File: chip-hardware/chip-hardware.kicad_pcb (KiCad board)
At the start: 2 copper layers, 74.2 x 30.5 mm, 22 parts, among them J1 Barrel_Jack, J2 Screw_Terminal_01x02, J3 Conn_01x02, U1 TLV70033_SOT23-5, U2 LIS3DH, U3 INA260, U4 MCP9808_MSOP, U5 ESP32-WROOM-32

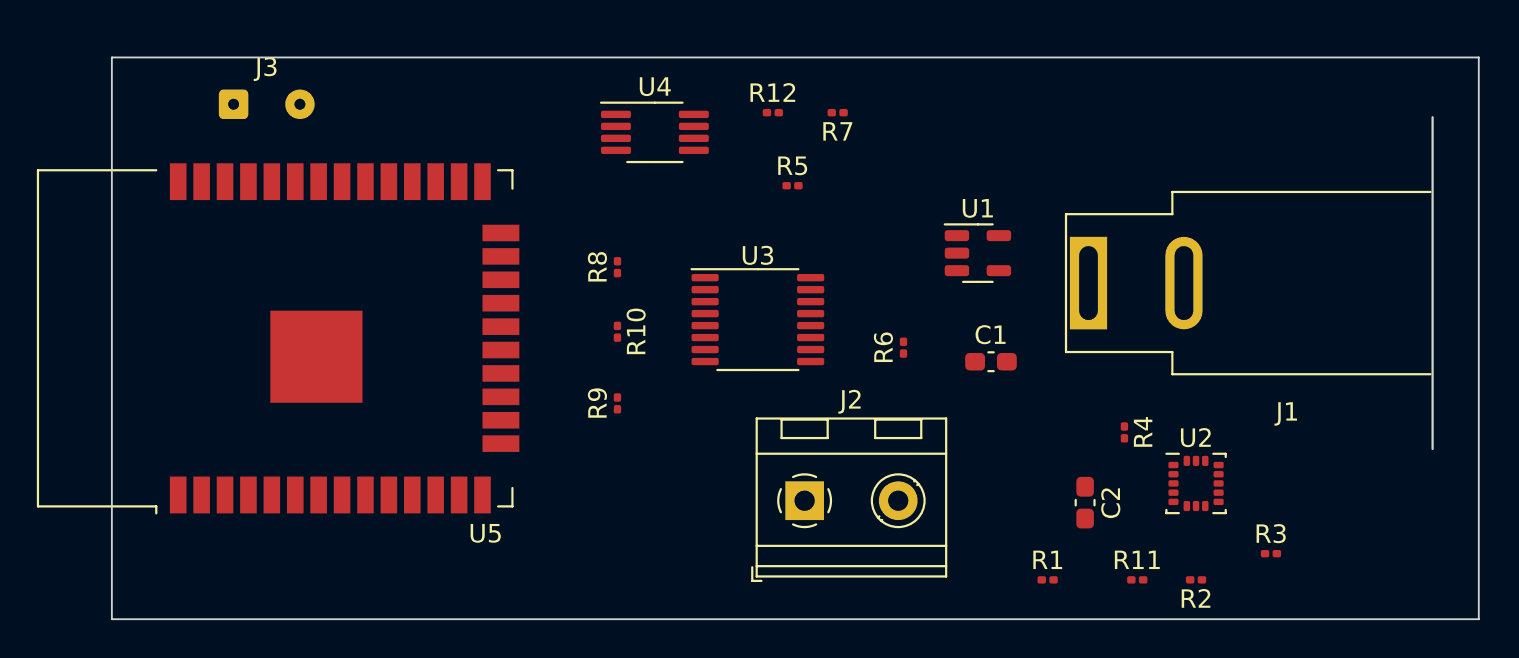
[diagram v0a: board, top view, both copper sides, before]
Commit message: Added corner radius to the chip
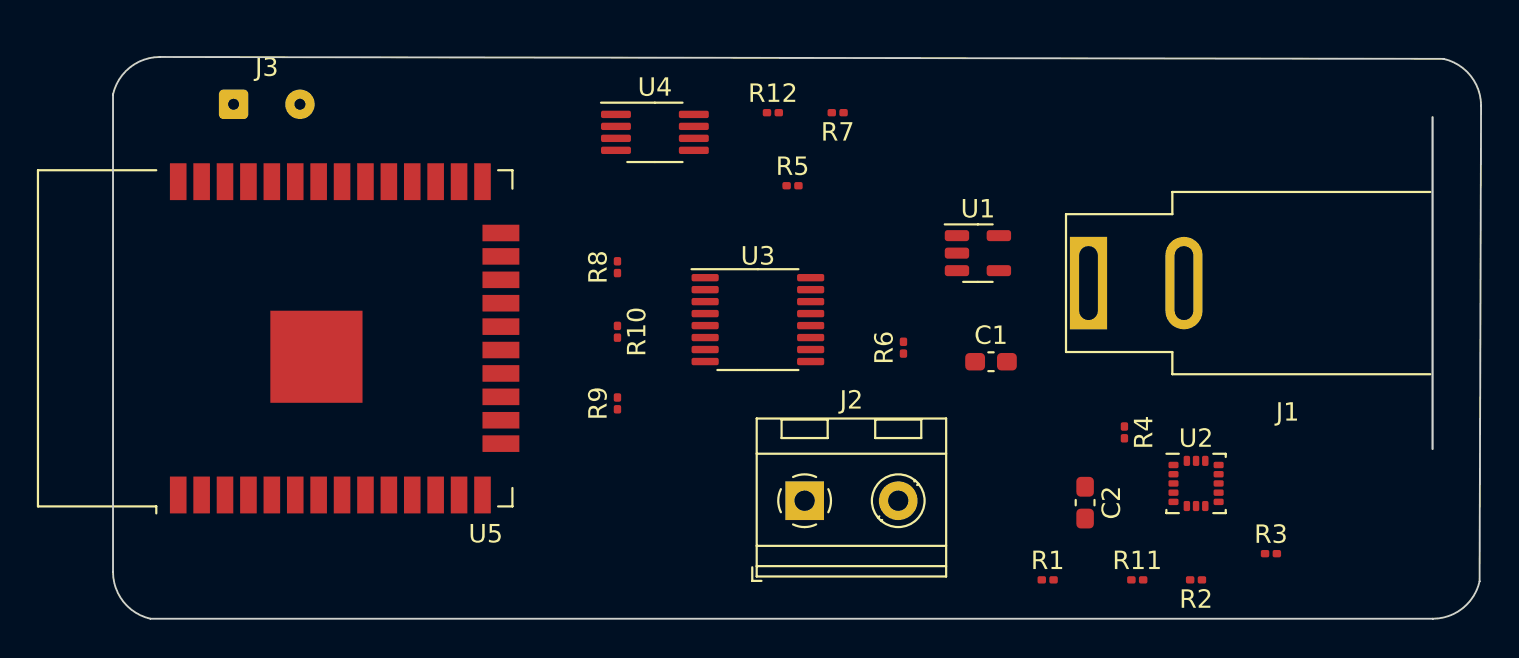
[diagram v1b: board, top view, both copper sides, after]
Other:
- outline, holes or cut-outs redrawn
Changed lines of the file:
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@@
     )
   )
-  (gr_rect (start 116.5246 86.1314) (end 190.6926 116.6114) (layer "Edge.Cuts") (width 0.1) (fill none))
+  (gr_arc (start 188.784508 86.208394) (mid 190.246 87.122) (end 190.816508 88.748394) (layer "Edge.Cuts") (width 0.1))
+  (gr_arc (start 190.735949 114.554) (mid 189.822343 116.015492) (end 188.195949 116.586) (layer "Edge.Cuts") (width 0.1))
+  (gr_arc (start 118.618 116.586) (mid 117.156508 115.672394) (end 116.586 114.046) (layer "Edge.Cuts") (width 0.1))
+  (gr_line (start 116.586 114.046) (end 116.586 88.138) (layer "Edge.Cuts") (width 0.1))
+  (gr_line (start 188.195949 116.586) (end 118.618 116.586) (layer "Edge.Cuts") (width 0.1))
+  (gr_line (start 190.735949 114.554) (end 190.816508 88.748394) (layer "Edge.Cuts") (width 0.1))
+  (gr_line (start 119.126 86.106) (end 188.784508 86.208394) (layer "Edge.Cuts") (width 0.1))
+  (gr_arc (start 116.586 88.138) (mid 117.499606 86.676508) (end 119.126 86.106) (layer "Edge.Cuts") (width 0.1))
 )

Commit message: more placement of parts
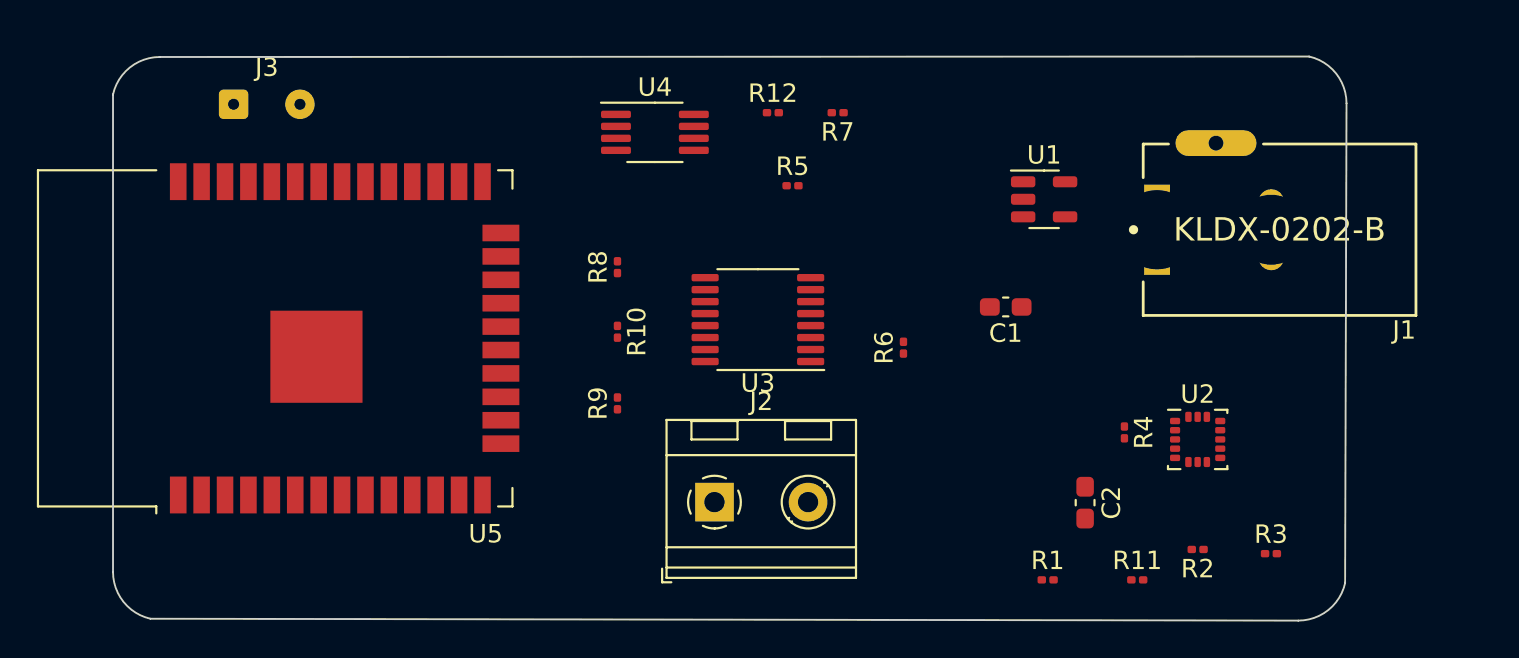
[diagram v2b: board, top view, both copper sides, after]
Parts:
- J1: value Barrel_Jack -> KLDX-0202-B; footprint Connector_BarrelJack:BarrelJack_SwitchcraftConxall_RAPC10U_Horizontal -> eec:Kycon-KLDX-0202-B-MFG
- moved J1 10.8 mm to (179.9, 95.5)
- moved J2 4.89 mm to (149.2, 110.3)
- moved U1 4.63 mm to (167.1, 93.8)
- moved C1 3.08 mm to (165.0, 99.7), turned to 180 degrees
- moved U2 2.39 mm to (175.4, 106.9)
- moved R2 1.65 mm to (175.4, 112.8)
- turned U3 to 180 degrees
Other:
- board size 74.2 x 30.5 mm -> 66.9 x 30.6 mm

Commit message: Got the traces mostly done. Just need to do some reviewing
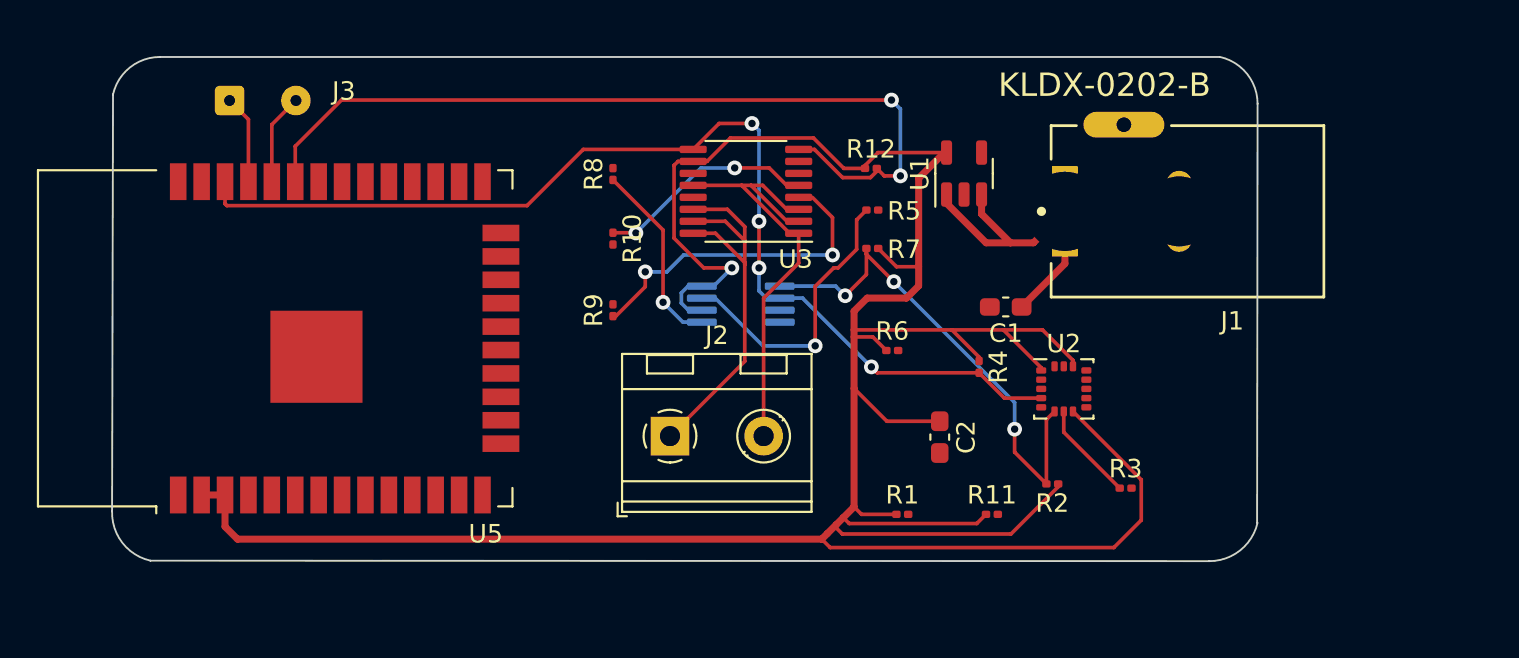
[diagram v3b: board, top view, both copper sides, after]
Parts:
- U4: moved to B.Cu
- moved U4 10.4 mm to (150.6, 99.5), turned to 180 degrees
- moved R2 8.65 mm to (167.6, 109.3)
- moved R1 8.65 mm to (159.4, 110.9)
- moved R3 8.65 mm to (171.5, 109.5)
- moved C2 8.65 mm to (161.4, 106.7)
- moved R11 8.65 mm to (164.3, 110.9)
- moved R4 8.65 mm to (163.6, 102.9)
- moved U2 7.77 mm to (168.2, 104.1)
- moved R7 7.60 mm to (157.8, 96.5)
- moved U3 6.99 mm to (150.9, 93.4)
- moved R12 6.12 mm to (157.7, 92.2)
- moved J1 5.09 mm to (174.9, 94.5)
- moved R9 5.06 mm to (143.7, 99.8)
- moved R10 5.06 mm to (143.7, 96.0)
- moved R8 5.06 mm to (143.7, 92.5)
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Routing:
- net +3V3: track 0.00 -> 168.1 mm, vias 0 -> 1
- net /SDA: track 0.00 -> 74.0 mm, vias 0 -> 5
- net /SCL: track 0.00 -> 58.6 mm, vias 0 -> 4
- net Net-(J2-Pad2): track 0.00 -> 25.6 mm
- net Net-(J2-Pad1): track 0.00 -> 23.0 mm
- net Net-(C1-Pad1): track 0.00 -> 17.9 mm
- net Net-(R9-Pad1): track 0.00 -> 17.3 mm, vias 0 -> 2
- net Net-(R5-Pad1): track 0.00 -> 15.9 mm, vias 0 -> 1
- net Net-(R10-Pad1): track 0.00 -> 11.9 mm, vias 0 -> 2
- net Net-(R8-Pad1): track 0.00 -> 10.3 mm, vias 0 -> 1
- net Net-(R3-Pad1): track 0.00 -> 5.42 mm
- net Net-(J3-Pad2): track 0.00 -> 4.94 mm
- net Net-(J3-Pad1): track 0.00 -> 4.83 mm
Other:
- board size 66.9 x 30.6 mm -> 62.2 x 27.4 mm

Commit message: filled the zones
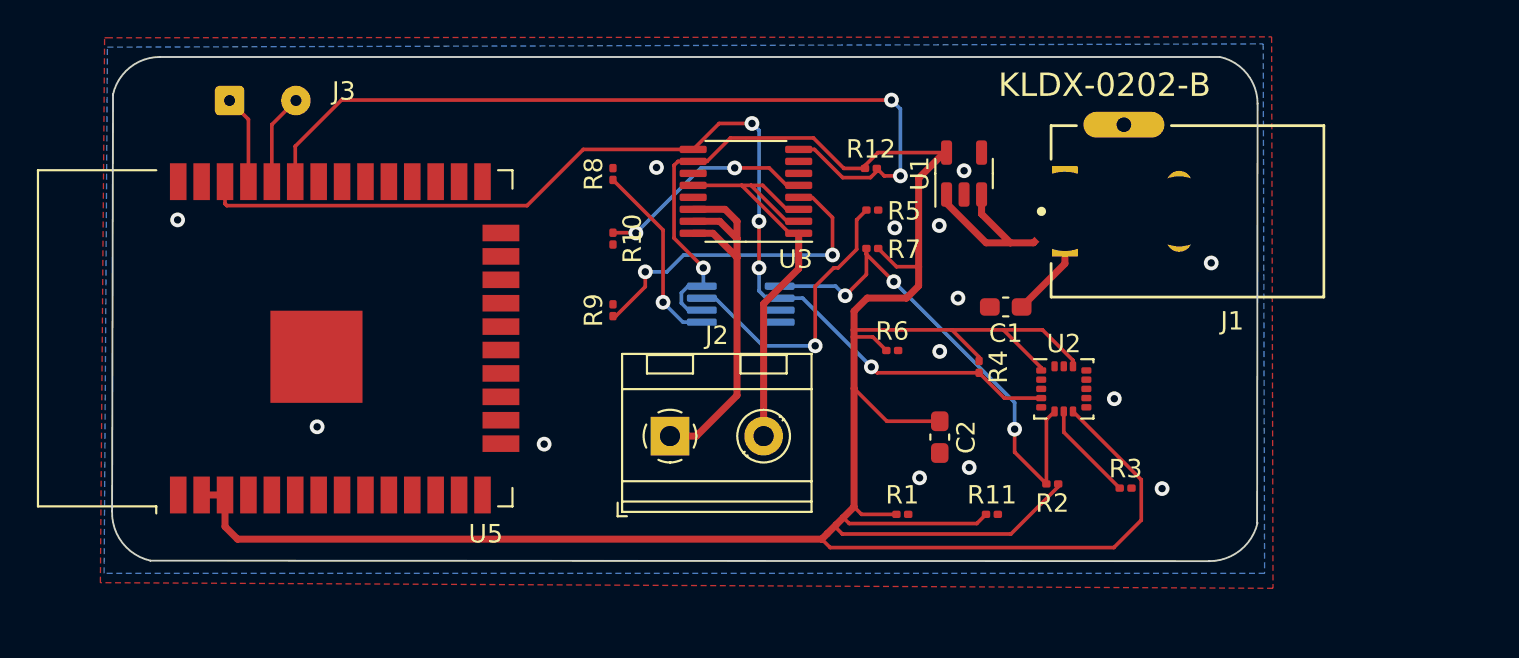
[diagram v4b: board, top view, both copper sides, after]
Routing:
- net +3V3: track 168.1 -> 165.6 mm
- net Net-(J2-Pad1): track 23.0 -> 22.3 mm
- net GND: vias 0 -> 13
- net (no net): vias 0 -> 1
- added copper zone on B.Cu, net GND
- added copper zone on F.Cu, net GND

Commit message: fixing some buggs
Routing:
- net GND: track 0.00 -> 29.3 mm, vias 13 -> 19
- net /SCL: track 58.6 -> 70.4 mm
- net +3V3: track 165.6 -> 174.0 mm
- net /SDA: track 74.0 -> 78.7 mm, vias 5 -> 6
- net (no net): vias 1 -> 0
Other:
- outline, holes or cut-outs redrawn

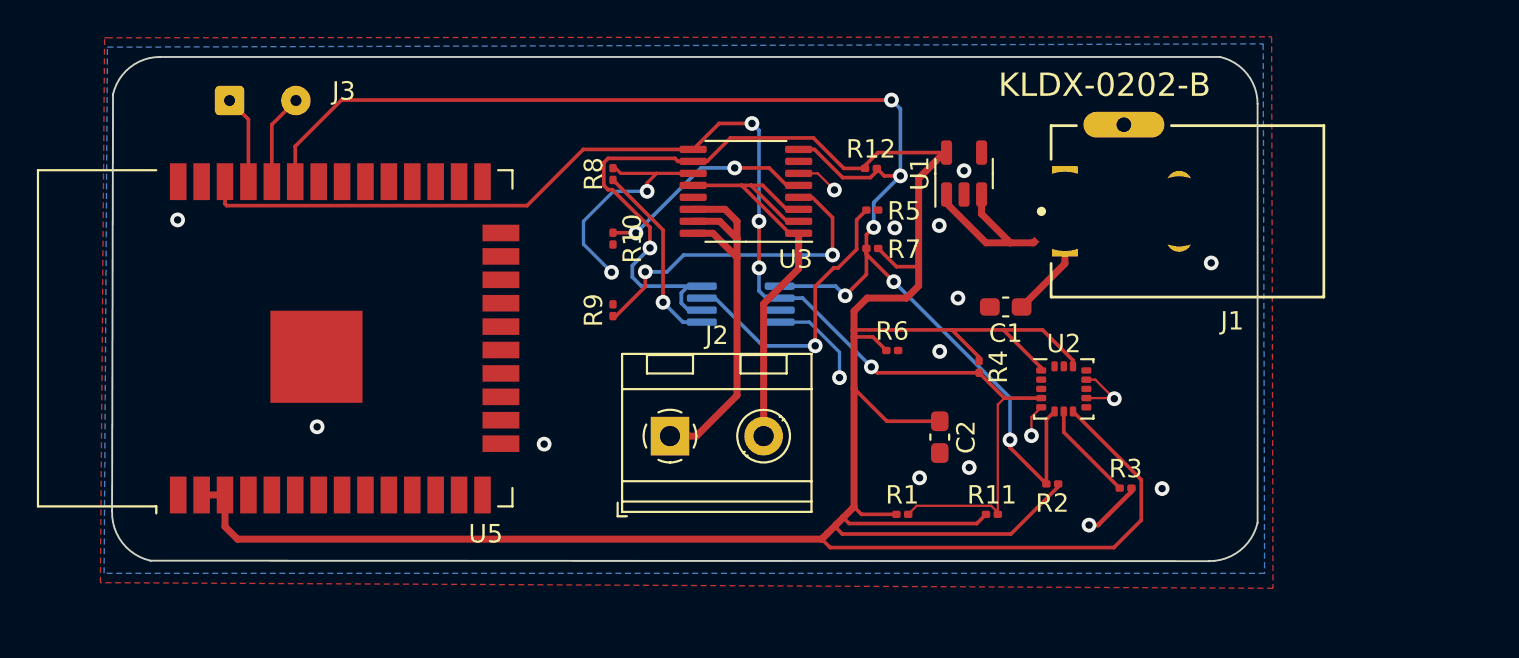
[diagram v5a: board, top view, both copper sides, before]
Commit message: Fixed resistor sizing. Accidentally selected 204 and not 603s. Would have been IMPOSSIBLE to solder
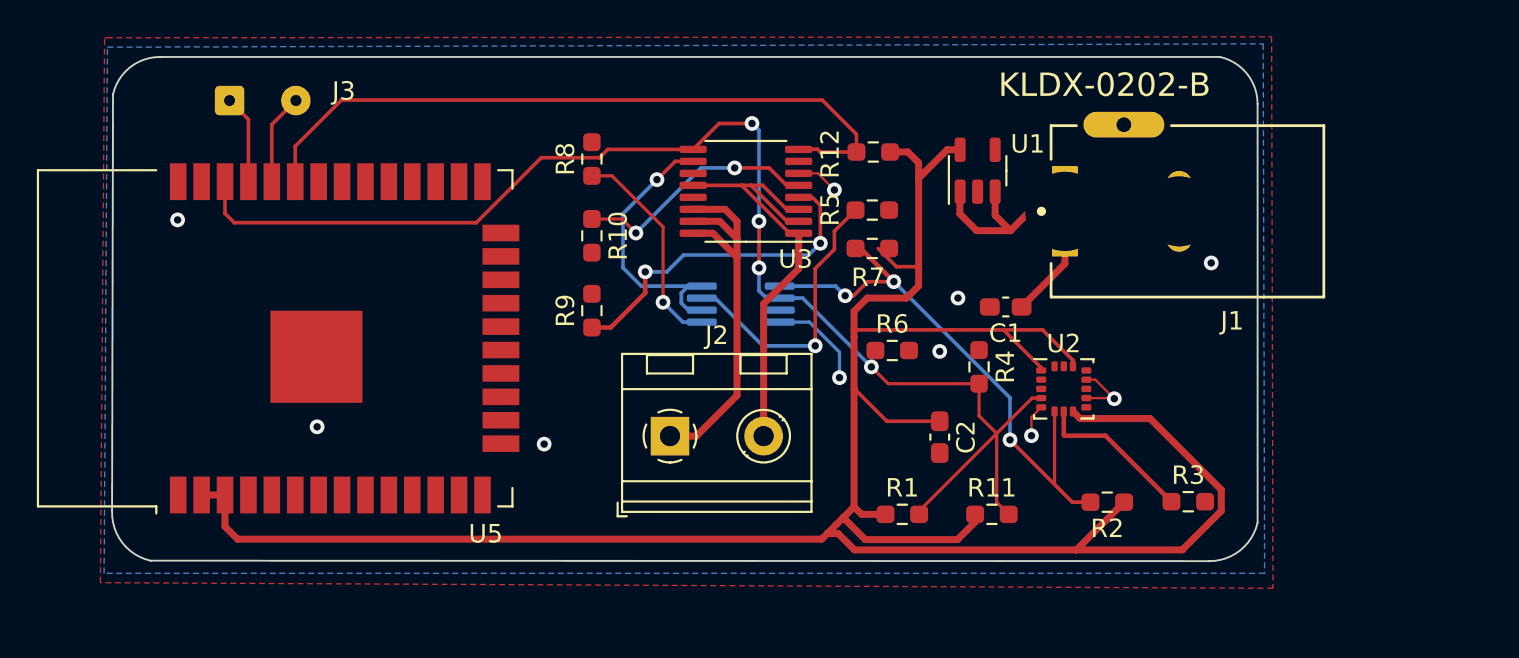
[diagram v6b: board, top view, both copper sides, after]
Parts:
- R1, R10, R11, R12, R2, R3, R4, R5, R6, R7, R8, R9: footprint Resistor_SMD:R_0201_0603Metric -> Resistor_SMD:R_0603_1608Metric_Pad0.98x0.95mm_HandSolder
- moved R3 3.48 mm to (174.9, 110.2)
- moved R2 3.14 mm to (170.5, 110.3)
- moved R8 1.40 mm to (142.6, 91.6)
- moved R10 1.15 mm to (142.6, 95.8)
- moved R9 1.14 mm to (142.6, 99.9)
- moved R12 0.90 mm to (157.8, 91.3), turned to 180 degrees
- moved U1 0.75 mm to (163.5, 92.3)
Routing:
- net +3V3: track 174.0 -> 151.3 mm
- net GND: track 29.3 -> 12.8 mm, vias 19 -> 10
- net /SDA: track 78.7 -> 70.2 mm, vias 6 -> 3
- net Net-(R3-Pad1): track 5.42 -> 8.61 mm
- net /SCL: track 70.4 -> 73.1 mm
- net Net-(C1-Pad1): track 17.9 -> 16.3 mm
- net Net-(R10-Pad1): track 11.9 -> 13.4 mm
- net Net-(R8-Pad1): track 10.3 -> 11.6 mm

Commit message: wired in all connecitions. Everything is looking good
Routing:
- net +3V3: track 151.3 -> 175.8 mm, vias 1 -> 2
- net GND: track 12.8 -> 19.8 mm, vias 10 -> 14
- net /SDA: track 70.2 -> 76.1 mm
- net Net-(R5-Pad1): track 15.5 -> 16.2 mm

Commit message: Circuit has no errors and looks good. Think it may be ready for submission
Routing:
- net +3V3: track 175.8 -> 175.2 mm
- net GND: vias 14 -> 17
